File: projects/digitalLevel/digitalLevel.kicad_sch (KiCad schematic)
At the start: 5 parts, among them J1 Conn_01x04_Socket, SW1 SW_DIP_x02, SW2 SW_DIP_x02, U1 XIAO-RP2040-DIP

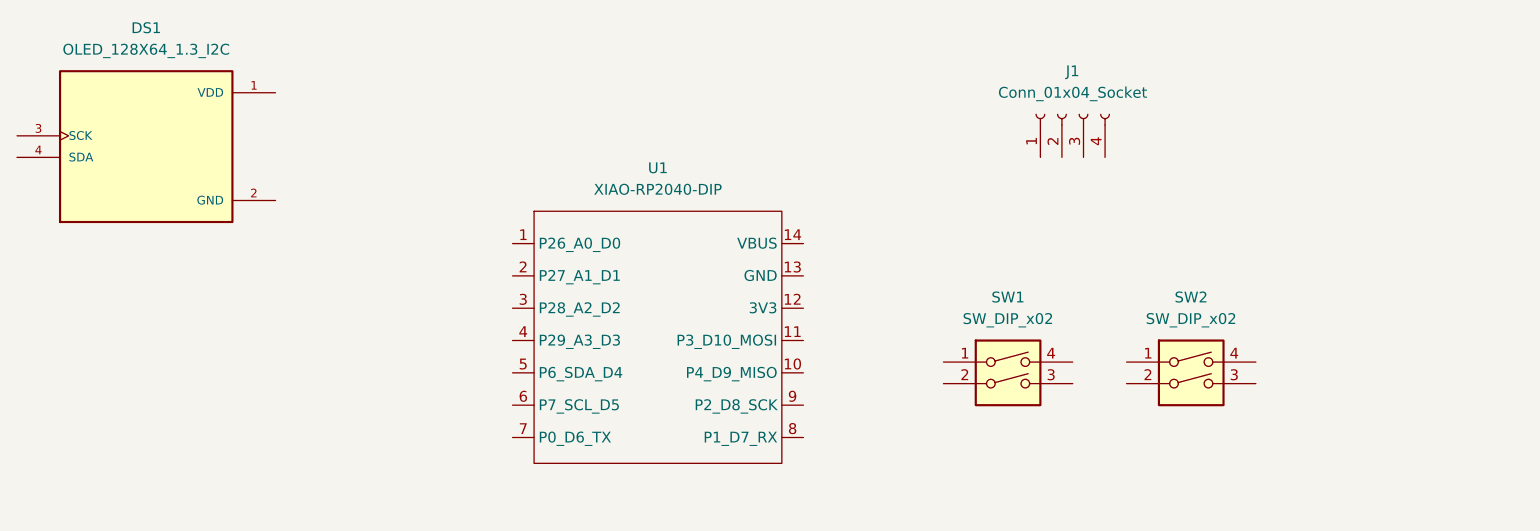
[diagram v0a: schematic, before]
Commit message: feat: Fix PCB size and export Gerber
- Changed the size of the digital level
pcb to be 6.75"x1.125" from 8.75"x1.125".

- Generate Gerber files for the board
to get manufactured

- Generate 3D .step model to model
case around

- Create footprint and symbol for
AAA battery pads
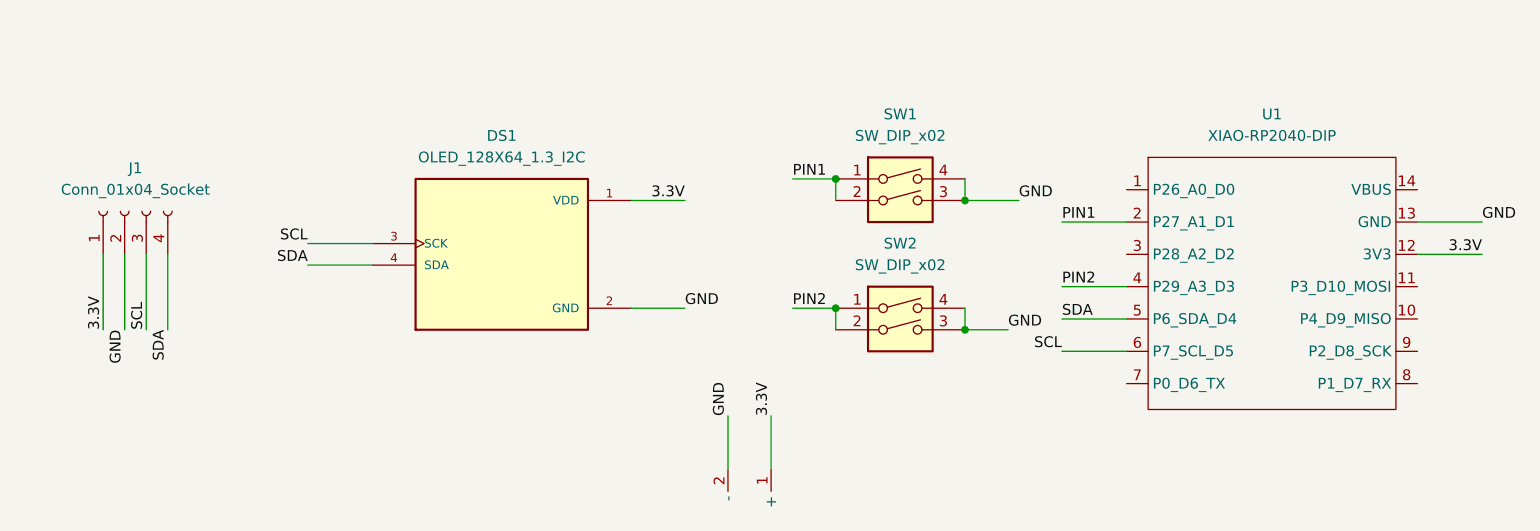
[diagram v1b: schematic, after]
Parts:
- added U2: (no value), Custom Footprints:2xAAABattery, symbol RP2040:AAABattery
- SW1, SW2: footprint Button_Switch_THT:SW_PUSH_6mm -> Button_Switch_THT:SW_PUSH_6mm_H5mm
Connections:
- net 3.3V: now reaches J1.1 (Pin_1)
- net 3.3V: now also DS1.1 (VDD), U1.12 (3V3), U2.1 (+)
- net GND: now reaches J1.2 (Pin_2)
- net GND: now also DS1.2 (GND), SW1.3, SW1.4, SW2.3, SW2.4, U1.13 (GND), U2.2 (-)
- net SCL: now reaches J1.3 (Pin_3)
- net SCL: now also DS1.3 (SCK), U1.6 (P7_SCL_D5)
- net SDA: now reaches J1.4 (Pin_4)
- net SDA: now also DS1.4 (SDA), U1.5 (P6_SDA_D4)
- net PIN1: now reaches SW1.1
- net PIN1: now also SW1.2, U1.2 (P27_A1_D1)
- net PIN2: now reaches U1.4 (P29_A3_D3)
- net PIN2: now also SW2.1, SW2.2
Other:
- moved on the sheet: DS1, J1, SW1, SW2, U1
